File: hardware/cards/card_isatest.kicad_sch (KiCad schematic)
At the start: 51 parts, among them J1 ISA slot (8-bit), J2 ISA SIDECAR, J3 5V jack, M1 Pico (RP2040), Q1 Q_PMOS, Q2 2N3904, U1 74LVC245A, U10 74HC595, U11 74HC595, U12 74HC595, U13 74HC165, U14 74HC165, U15 74HCT74, U16 74HC161, U17 74HC157, U18 74HC157, U19 74HCT04, U2 74LVC245A, U3 74LVC245A, U4 74LVC245A, U5 74LVC245A, U6 74LVC245A, U7 74LVC245A, U8 74LVC245A, U9 74HC595

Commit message: Design review 2026-07-11: rail protection, decoupling, wiring fixes
Protection:
- Sidecar +5V now feeds through a 2A polyfuse into +5V_ISA with an
  SMBJ5.0A clamp + 22uF bulk (a faulted ISA card trips its own fuse
  instead of dropping the board; back-fed voltage is clamped).
- USB-C VBUS enters through a 3A polyfuse with an SMBJ5.0A on +5V
  (backstop for the CFG1 9-20V failure mode). CH224K gains a 1uF VDD
  cap; its PG routes to Supervisor GPIO16 as PD_PG. Buck output
  doubled to 2x22uF, 10uF at VIN, extra rail bulk.
- Supervisor USB-A host port: 27R series termination (RP2040
  requirement), USBLC6-2SC6 ESD array, 100uF VBUS bulk.
- Video: HDMI +5V fused (500mA), HPD sensed on GPIO41, 100R series on
  VGA sync. TMDS ESD array deferred to layout (no symbol).
- card_isatest: V5RAW bulk, Q1 gate soft-start cap, TVS on DUT rail.

Wiring fixes:
- SPKR had no driver anywhere (netlist: 1 node). Bus MCU GPIO22
  reassigned from the diagnostics-only bus-CLK sense to SPKR; bus_mcu
  drops CLK from its interface. Doc 5.2 updated.
- bus_mcu C8 decoupled +3V3, a rail that sheet never uses -> 3V3_BUS.
- Storage IRQ5 was push-pull (permanently driven when idle) -> 2N7002
  + gated '125 tri-state, same convention as the LPT IRQ7 stage.
- MAX3241 pump caps resized to the 5V datasheet values (47nF/330nF).
- LPT DB25 status inputs get 4.7k pull-ups (floated with no printer).
- Audio line-out gets a 100R series isolator before the jack.

Best practices:
- Decoupling to ~1x100nF per IC on every sheet + bulk per board
  (cpu_core 7->16 incl. the naked 3.3V oscillator, storage 4->11,
  parallel 6->13, rtc/com/video/bus_mcu/card_isatest similar).
- All floating spare CMOS inputs tied ('00/'74/'157/'02/'04/'125
  sections across cpu_core, bus_mcu, rtc, storage, card_isatest).

Sourcing: new parts mapped in parts.py with JLC-verified LCSC numbers;
Power_Protection lib registered in the tools; TPS563200 stock alert
(4 pcs left at JLC) flagged in parts.py + jlcpcb-sourcing.md. All
decisi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
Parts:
- removed R1, R2, R3: 10k, symbol Device:R
- removed U19: 74HCT04, symbol mini-xt:74HCT04
- added C11, C12, C13, C14, C15, C16, C17, C8: 100nF, symbol Device:C
- added D1: D_Schottky, symbol Device:D_Schottky
- added R11, R12, R13, R14, R15: 10k, symbol Device:R
- C10: renamed from R12; value 10k -> 100nF; symbol Device:R -> Device:C; LCSC Part Num C25804 -> C14663
- C9: renamed from R11; value 10k -> 22uF; symbol Device:R -> Device:C_Polarized; LCSC Part Num C25804 -> C12891
- D3: renamed from R13; value 10k -> SMBJ5.0A; symbol Device:R -> Device:D_Zener; LCSC Part Num C25804 -> C19077558
- R3: renamed from C8; value 100nF -> 10k; symbol Device:C -> Device:R; LCSC Part Num C14663 -> C25804
- U19: renamed from D1; value D_Schottky -> 74HCT04; symbol Device:D_Schottky -> mini-xt:74HCT04; LCSC Part Num C8678 -> C672096
- renumbered R14 to R1, R15 to R2
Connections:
- net +3V3: now also R1.2, C11.1, C12.1, C13.1, C14.1, C15.1, C16.1
- net +5V: now also D3.1 (K), R2.2, C8.1; no longer R3.1
- net CLK: now also U19.2 (P2)
- net CLKSRC_INV: now also U19.8 (P8)
- net CLK_PRE: now also U19.1 (P1)
- net CLK_SRC: now also U19.9 (P9)
- net DIV3_LD: now also U19.4 (P4)
- net DIV3_TC: now also U19.3 (P3)
- net DRQ1: now also R13.1; no longer D3.1
- net DRQ2: now also R14.1; no longer R1.1
- net DRQ3: now also R15.1; no longer R2.1
- net DUT_PWR_EN: now also R3.1
- net GND: now also U15.11 (C), U15.12 (D), U17.10 (I1c), U17.11 (I0c), U17.13 (I1d), U17.14 (I0d), U17.5 (I0b), U17.6 (I1b), U18.10 (I1c), U18.11 (I0c), U18.13 (I1d), U18.14 (I0d), U18.5 (I0b), U18.6 (I1b), U19.7 (GND), C11.2, C12.2, C13.2, C14.2, C15.2, C16.2, C17.2, C8.2, R11.2, R12.2, R13.2, R14.2, R15.2; no longer C10.2, R1.2, R2.2
- net IOCHRDY: now also R2.1
- net IRQ7: now also R11.1; no longer C9.1
- net IRQ8: now also R12.1; no longer C10.1
- net OSC: now also U19.12 (P12)
- net OSC_3V3: now also U19.13 (P13)
- net PFET_G: now also C10.2
- net PIO_CLK: now also U19.11 (P11)
- net PIO_CLK_5V: now also U19.10 (P10)
- net SPEED_INV: now also U19.6 (P6)
- net SPEED_SEL: now also U19.5 (P5)
- net V5RAW: now also C10.1, C9.1, U15.10 (~{S}), U15.13 (~{R}), U19.14 (VCC), C17.1, D1.1 (K); no longer U19.1 (K)
- net VEXT: now also D1.2 (A); no longer U19.2 (A)
- net ~{BUF_EN}: now also R1.1
- no-connect marks 37 -> 45
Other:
- note added: "Power: USB 5V (logic) + external jack (bus/DUT) OR-ed via D1/D2 to V5RAW; Q1 P-FET switches bus +5V. Soft-start: C10 ramps Q1 gate. DUT rail protected by bulk C9 + TVS clamp D3. Gate pulled to V5RAW (off), pulled low by Q2 NPN when DUT_PWR_EN=1."
- note removed: "Power: USB 5V (logic) + external jack (bus/DUT) OR-ed via D1/D2 to V5RAW; Q1 P-FET switches bus +5V. Gate pulled to V5RAW (off), pulled low by Q2 NPN when DUT_PWR_EN=1."
- moved on the sheet: R1, R2

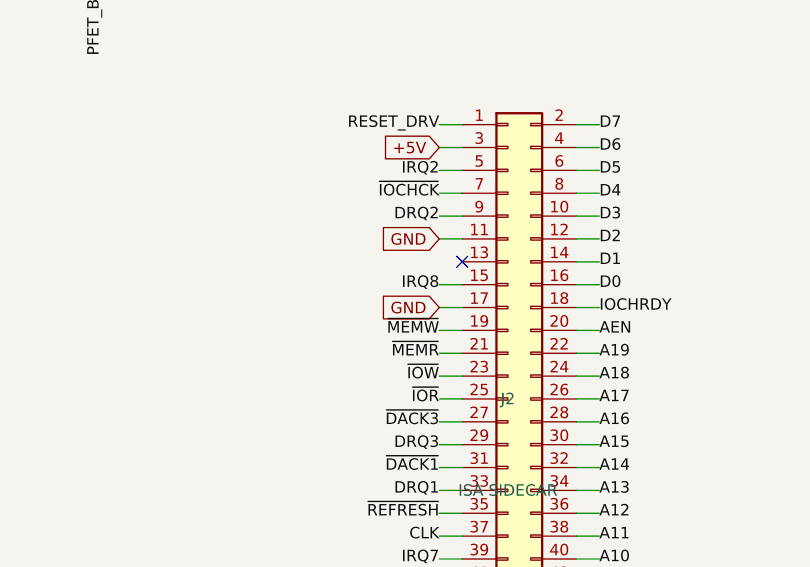
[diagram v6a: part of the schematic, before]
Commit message: Design-review fixes: reset parking, IRQ8 off the header, analog cleanups
Netlist-wide review sweep. IRQ8 leaves the 60-pin ISA header (pin 15 is a
second GND return; the on-board RTC owns IRQ8 exclusively, so its push-pull
drive is now correct by construction). Bus MCU Hi-Z parking completed:
~CPURESET pulled low (V20 held in reset while the MCU is unprogrammed),
~DACK1/~REFRESH parked deasserted, DRQ1 idled low. Supervisor 12 MHz crystal
damping R actually in series now (was parallel-to-nothing), plus a second
USBLC6 so both prog-port SW2 positions are ESD-protected. Audio: 0.5x PG
summing (MCP6002 headroom), 100k LINE bleed, unit B parked as a follower --
and the SUM stub moved off pin 5's row, where wiring unit B would have
silently merged SUM into VREF. CH224K VDD fed through 1k per the WCH ref
design. VGA blue ladder rescaled 1k/510 -> 820/470 (was ~12% blue-deficient).
Spare CMOS gate inputs grounded uniformly (cpu_core/rtc/storage); UART_RXD
pulled up (SIN idles at mark with JP1 open); dead pins/parts dropped
(com_port CLK, parallel RESET_DRV, storage R3). Bus CLK fixed at 7.16 MHz
logged as a decision. New passives mapped to JLC basic parts in parts.py.

Co-Authored-By: Claude Fable 5 <noreply@anthropic.com>
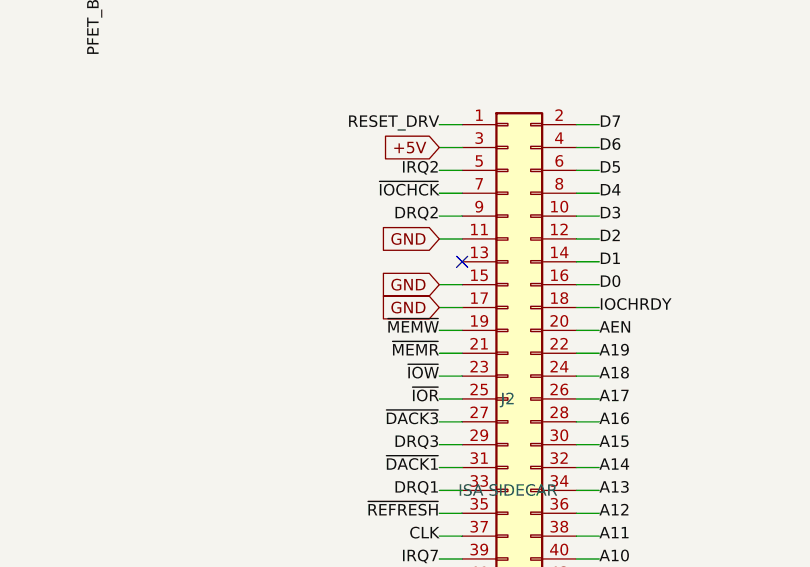
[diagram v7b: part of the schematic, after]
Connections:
- net GND: now also J2.15 (Pin_15)
- net IRQ8: no longer J2.15 (Pin_15)
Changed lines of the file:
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@@
 		)
 	)
-	(label "IRQ8"
+	(global_label "GND"
+		(shape input)
 		(at 563.88 134.62 180)
 		(effects

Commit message: Parts: footprints for all components, close 6 LCSC map gaps, check_parts.py
- mxsch.py emits the Footprint property from component props (was
  hard-coded empty); parts.py entries now carry a verified KiCad
  footprint, applied at build time alongside the LCSC number.
- Map keys fixed to match placed values: USB_PROG, SS34, LED (PicoGUS),
  APS6404L, CB3T3257/45 -- every combo across all sheets + cards now
  resolves (130 combos, 455 netlist components, all with footprints).
- Package corrections from JLC DB re-check: RTL8019AS is QFP-100 14x20
  P0.65 (not TQFP); C2897411 female header is a 2x10 strip -- fine for
  Core2350B, Pico needs 2x 1x20 (noted in jlcpcb-sourcing.md).
- 10 mini-xt:* placeholder footprints mark parts whose land pattern is
  authored at layout from the EasyEDA data (CH224K, magnetics, RJ45,
  HDMI, CF socket, ISA slot, switches, Core2350B PGA).
- New tools/check_parts.py: fails on unmapped combos, missing fp
  fields, or footprints absent from the installed KiCad libs.

Co-Authored-By: Claude Fable 5 <noreply@anthropic.com>
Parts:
- C1, C10, C11, C12, C13, C14, C15, C16, C17, C2, C3, C4, C5, C6, C7, C8: footprint (none) -> Capacitor_SMD:C_0603_1608Metric
- C9: footprint (none) -> Capacitor_SMD:C_1206_3216Metric
- D1, D2: footprint (none) -> Diode_SMD:D_SMA
- D3: footprint (none) -> Diode_SMD:D_SMB
- J1: footprint (none) -> mini-xt:ISA_Slot_8bit_EdgeSocket
- J2: footprint (none) -> Connector_PinHeader_2.54mm:PinHeader_2x30_P2.54mm_Vertical
- J3: footprint (none) -> Connector_BarrelJack:BarrelJack_Horizontal
- M1: footprint (none) -> Module:RaspberryPi_Pico_Common_THT
- OSC1: footprint (none) -> Oscillator:Oscillator_SMD_EuroQuartz_XO32-4Pin_3.2x2.5mm
- Q1, Q2: footprint (none) -> Package_TO_SOT_SMD:SOT-23
- R1, R10, R11, R12, R13, R14, R15, R2, R3, R4, R5, R6, R7, R8, R9: footprint (none) -> Resistor_SMD:R_0603_1608Metric
- U1, U2, U3, U4, U5, U6, U7, U8: footprint (none) -> Package_SO:TSSOP-20_4.4x6.5mm_P0.65mm
- U10, U11, U12, U13, U14, U16, U17, U18, U9: footprint (none) -> Package_SO:SOIC-16_3.9x9.9mm_P1.27mm
- U15, U19: footprint (none) -> Package_SO:SOIC-14_3.9x8.7mm_P1.27mm
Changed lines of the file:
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@@
 			)
 		)
-		(property "Footprint" ""
+		(property "Footprint" "Module:RaspberryPi_Pico_Common_THT"
 			(at 101.6 152.4 0)
 			(effects
@@
 			)
 		)
-		(property "Footprint" ""
+		(property "Footprint" "Package_SO:TSSOP-20_4.4x6.5mm_P0.65mm"
 			(at 203.2 76.2 0)
 			(effects
@@
 			)
 		)
-		(property "Footprint" ""
+		(property "Footprint" "Package_SO:TSSOP-20_4.4x6.5mm_P0.65mm"
 			(at 203.2 152.4 0)
 			(effects
@@
 			)
 		)
-		(property "Footprint" ""
+		(property "Footprint" "Package_SO:TSSOP-20_4.4x6.5mm_P0.65mm"
 			(at 279.4 152.4 0)
 			(effects
@@
 			)
 		)
-		(property "Footprint" ""
+		(property "Footprint" "Package_SO:TSSOP-20_4.4x6.5mm_P0.65mm"
 			(at 355.6 152.4 0)
 			(effects
@@
 			)
 		)
-		(property "Footprint" ""
+		(property "Footprint" "Package_SO:TSSOP-20_4.4x6.5mm_P0.65mm"
 			(at 203.2 228.6 0)
 			(effects
@@
 			)
 		)
-		(property "Footprint" ""
+		(property "Footprint" "Package_SO:TSSOP-20_4.4x6.5mm_P0.65mm"
 			(at 279.4 228.6 0)
 			(effects
@@
 			)
 		)
-		(property "Footprint" ""
+		(property "Footprint" "Package_SO:TSSOP-20_4.4x6.5mm_P0.65mm"
 			(at 355.6 228.6 0)
 			(effects
@@
 			)
 		)
-		(property "Footprint" ""
+		(property "Footprint" "Package_SO:TSSOP-20_4.4x6.5mm_P0.65mm"
 			(at 431.8 228.6 0)
 			(effects
@@
 			)
 		)
-		(property "Footprint" ""
+		(property "Footprint" "Capacitor_SMD:C_0603_1608Metric"
 			(at 190.5 40.64 0)
 			(effects
@@
 			)
 		)
-		(property "Footprint" ""
+		(property "Footprint" "Capacitor_SMD:C_0603_1608Metric"
 			(at 355.6 40.64 0)
 			(effects
@@
 			)
 		)
-		(property "Footprint" ""
+		(property "Footprint" "Package_SO:SOIC-16_3.9x9.9mm_P1.27mm"
 			(at 60.96 304.8 0)
 			(effects
@@
 			)
 		)
-		(property "Footprint" ""
+		(property "Footprint" "Package_SO:SOIC-16_3.9x9.9mm_P1.27mm"
 			(at 137.16 304.8 0)
 			(effects
@@
 			)
 		)
-		(property "Footprint" ""
+		(property "Footprint" "Package_SO:SOIC-16_3.9x9.9mm_P1.27mm"
 			(at 213.36 304.8 0)
 			(effects
@@
 			)
 		)
-		(property "Footprint" ""
+		(property "Footprint" "Package_SO:SOIC-16_3.9x9.9mm_P1.27mm"
 			(at 289.56 304.8 0)
 			(effects
@@
 			)
 		)
-		(property "Footprint" ""
+		(property "Footprint" "Capacitor_SMD:C_0603_1608Metric"
 			(at 60.96 274.32 0)
 			(effects
@@
 			)
 		)
-		(property "Footprint" ""
+		(property "Footprint" "Package_SO:SOIC-16_3.9x9.9mm_P1.27mm"
 			(at 365.76 304.8 0)
 			(effects
@@
 			)
 		)
-		(property "Footprint" ""
+		(property "Footprint" "Package_SO:SOIC-16_3.9x9.9mm_P1.27mm"
 			(at 441.96 304.8 0)
 			(effects
@@
 			)
 		)
-		(property "Footprint" ""
+		(property "Footprint" "Capacitor_SMD:C_0603_1608Metric"
 			(at 365.76 274.32 0)
 			(effects
@@
 			)
 		)
-		(property "Footprint" ""
+		(property "Footprint" "Oscillator:Oscillator_SMD_EuroQuartz_XO32-4Pin_3.2x2.5mm"
 			(at 60.96 45.72 0)
 			(effects
@@
 			)
 		)
-		(property "Footprint" ""
+		(property "Footprint" "Package_SO:SOIC-14_3.9x8.7mm_P1.27mm"
 			(at 137.16 45.72 0)
 			(effects
@@
 			)
 		)
-		(property "Footprint" ""
+		(property "Footprint" "Package_SO:SOIC-16_3.9x9.9mm_P1.27mm"
 			(at 213.36 45.72 0)
 			(effects
@@
 			)
 		)
-		(property "Footprint" ""
+		(property "Footprint" "Package_SO:SOIC-16_3.9x9.9mm_P1.27mm"
 			(at 60.96 106.68 0)
 			(effects
@@
 			)
 		)
-		(property "Footprint" ""
+		(property "Footprint" "Package_SO:SOIC-16_3.9x9.9mm_P1.27mm"
 			(at 137.16 106.68 0)
 			(effects
@@
 			)
 		)
-		(property "Footprint" ""
+		(property "Footprint" "Package_SO:SOIC-14_3.9x8.7mm_P1.27mm"
 			(at 213.36 106.68 0)
 			(effects
@@
 			)
 		)
-		(property "Footprint" ""
+		(property "Footprint" "Capacitor_SMD:C_0603_1608Metric"
 			(at 60.96 76.2 0)
 			(effects
@@
 			)
 		)
-		(property "Footprint" ""
+		(property "Footprint" "Connector_BarrelJack:BarrelJack_Horizontal"
 			(at 495.3 60.96 0)
 			(effects
@@
 			)
 		)
-		(property "Footprint" ""
+		(property "Footprint" "Diode_SMD:D_SMA"
 			(at 520.7 60.96 0)
 			(effects
@@
 			)
 		)
-		(property "Footprint" ""
+		(property "Footprint" "Diode_SMD:D_SMA"
 			(at 520.7 76.2 0)
 			(effects
@@
 			)
 		)
-		(property "Footprint" ""
+		(property "Footprint" "Package_TO_SOT_SMD:SOT-23"
 			(at 546.1 68.58 0)
 			(effects
@@
 			)
 		)
-		(property "Footprint" ""
+		(property "Footprint" "Resistor_SMD:R_0603_1608Metric"
 			(at 546.1 45.72 0)
 			(effects
@@
 			)
 		)
-		(property "Footprint" ""
+		(property "Footprint" "Package_TO_SOT_SMD:SOT-23"
 			(at 546.1 96.52 0)
 			(effects
@@
 			)
 		)
-		(property "Footprint" ""
+		(property "Footprint" "Resistor_SMD:R_0603_1608Metric"
 			(at 525.78 96.52 0)
 			(effects
@@
 			)
 		)
-		(property "Footprint" ""
+		(property "Footprint" "Capacitor_SMD:C_1206_3216Metric"
 			(at 508 91.44 0)
 			(effects
@@
 			)
 		)
-		(property "Footprint" ""
+		(property "Footprint" "Capacitor_SMD:C_0603_1608Metric"
 			(at 533.4 45.72 0)
 			(effects
@@
 			)
 		)
-		(property "Footprint" ""
+		(property "Footprint" "Diode_SMD:D_SMB"
 			(at 571.5 91.44 0)
 			(effects
@@
 			)
 		)
-		(property "Footprint" ""
+		(property "Footprint" "Resistor_SMD:R_0603_1608Metric"
 			(at 152.4 96.52 0)
 			(effects
@@
 			)
 		)
-		(property "Footprint" ""
+		(property "Footprint" "Resistor_SMD:R_0603_1608Metric"
 			(at 571.5 45.72 0)
 			(effects
@@
 			)
 		)
-		(property "Footprint" ""
+		(property "Footprint" "Resistor_SMD:R_0603_1608Metric"
 			(at 571.5 76.2 0)
 			(effects
@@
 			)
 		)
-		(property "Footprint" ""
+		(property "Footprint" "Resistor_SMD:R_0603_1608Metric"
 			(at 38.1 370.84 0)
 			(effects
@@
 			)
 		)
-		(property "Footprint" ""
+		(property "Footprint" "Resistor_SMD:R_0603_1608Metric"
 			(at 53.34 370.84 0)
 			(effects
@@
 			)
 		)
-		(property "Footprint" ""
+		(property "Footprint" "Resistor_SMD:R_0603_1608Metric"
 			(at 68.58 370.84 0)
 			(effects
@@
 			)
 		)
-		(property "Footprint" ""
+		(property "Footprint" "Resistor_SMD:R_0603_1608Metric"
 			(at 83.82 370.84 0)
 			(effects
@@
 			)
 		)
-		(property "Footprint" ""
+		(property "Footprint" "Resistor_SMD:R_0603_1608Metric"
 			(at 99.06 370.84 0)
 			(effects
@@
 			)
 		)
-		(property "Footprint" ""
+		(property "Footprint" "Resistor_SMD:R_0603_1608Metric"
 			(at 114.3 370.84 0)
 			(effects
@@
 			)
 		)
-		(property "Footprint" ""
+		(property "Footprint" "Resistor_SMD:R_0603_1608Metric"
 			(at 129.54 370.84 0)
 			(effects
@@
 			)
 		)
-		(property "Footprint" ""
+		(property "Footprint" "Resistor_SMD:R_0603_1608Metric"
 			(at 144.78 370.84 0)
 			(effects
@@
 			)
 		)
-		(property "Footprint" ""
+		(property "Footprint" "Resistor_SMD:R_0603_1608Metric"
 			(at 160.02 370.84 0)
 			(effects
@@
 			)
 		)
-		(property "Footprint" ""
+		(property "Footprint" "Resistor_SMD:R_0603_1608Metric"
 			(at 175.26 370.84 0)
 			(effects
@@
 			)
 		)
-		(property "Footprint" ""
+		(property "Footprint" "Capacitor_SMD:C_0603_1608Metric"
 			(at 490.22 91.44 0)
 			(effects
@@
 			)
 		)
-		(property "Footprint" ""
+		(property "Footprint" "Capacitor_SMD:C_0603_1608Metric"
 			(at 241.3 40.64 0)
 			(effects
@@
 			)
 		)
-		(property "Footprint" ""
+		(property "Footprint" "Capacitor_SMD:C_0603_1608Metric"
 			(at 302.26 40.64 0)
 			(effects
@@
 			)
 		)
-		(property "Footprint" ""
+		(property "Footprint" "Capacitor_SMD:C_0603_1608Metric"
 			(at 419.1 40.64 0)
 			(effects
@@
 			)
 		)
-		(property "Footprint" ""
+		(property "Footprint" "Capacitor_SMD:C_0603_1608Metric"
 			(at 137.16 274.32 0)
 			(effects
@@
 			)
 		)
-		(property "Footprint" ""
+		(property "Footprint" "Capacitor_SMD:C_0603_1608Metric"
 			(at 213.36 274.32 0)
 			(effects
@@
 			)
 		)
-		(property "Footprint" ""
+		(property "Footprint" "Capacitor_SMD:C_0603_1608Metric"
 			(at 441.96 274.32 0)
 			(effects
@@
 			)
 		)
-		(property "Footprint" ""
+		(property "Footprint" "Capacitor_SMD:C_0603_1608Metric"
 			(at 167.64 76.2 0)
 			(effects
@@
 			)
 		)
-		(property "Footprint" ""
+		(property "Footprint" "mini-xt:ISA_Slot_8bit_EdgeSocket"
 			(at 508 254 0)
 			(effects
@@
 			)
 		)
-		(property "Footprint" ""
+		(property "Footprint" "Connector_PinHeader_2.54mm:PinHeader_2x30_P2.54mm_Vertical"
 			(at 571.5 152.4 0)
 			(effects
@@
 			)
 		)
-		(property "Footprint" ""
+		(property "Footprint" "Capacitor_SMD:C_0603_1608Metric"
 			(at 40.64 50.8 0)
 			(effects
@@
 			)
 		)
-		(property "Footprint" ""
+		(property "Footprint" "Capacitor_SMD:C_0603_1608Metric"
 			(at 55.88 50.8 0)
 			(effects
